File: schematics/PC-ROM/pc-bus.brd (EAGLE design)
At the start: 152.4 x 138.4 mm, 20 parts

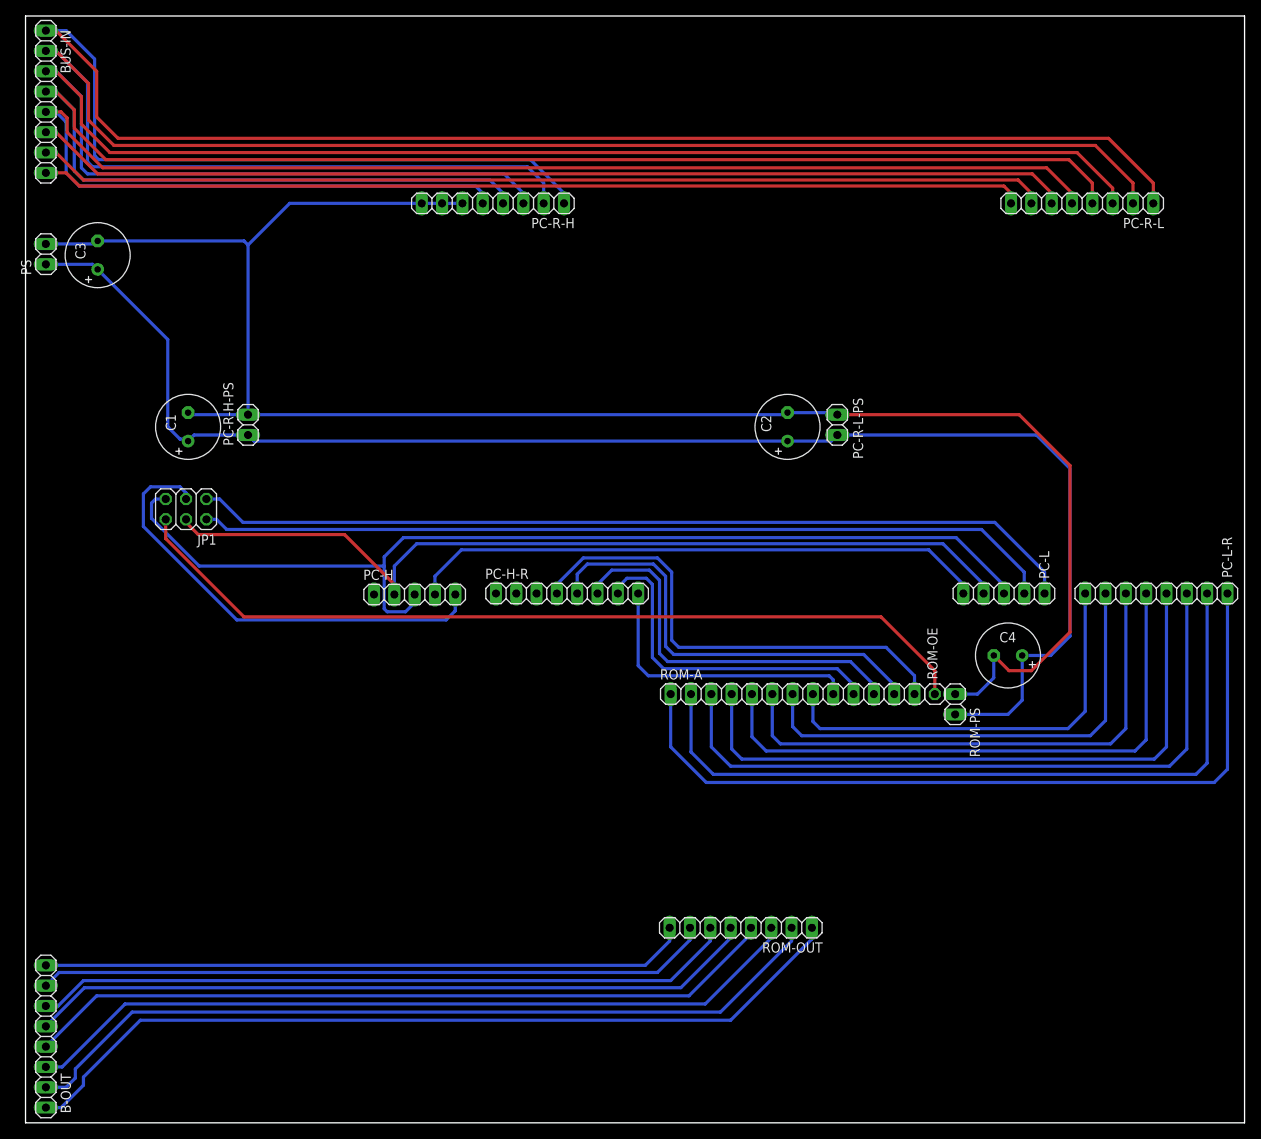
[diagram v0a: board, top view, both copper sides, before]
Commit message: Added resistors to rom address.
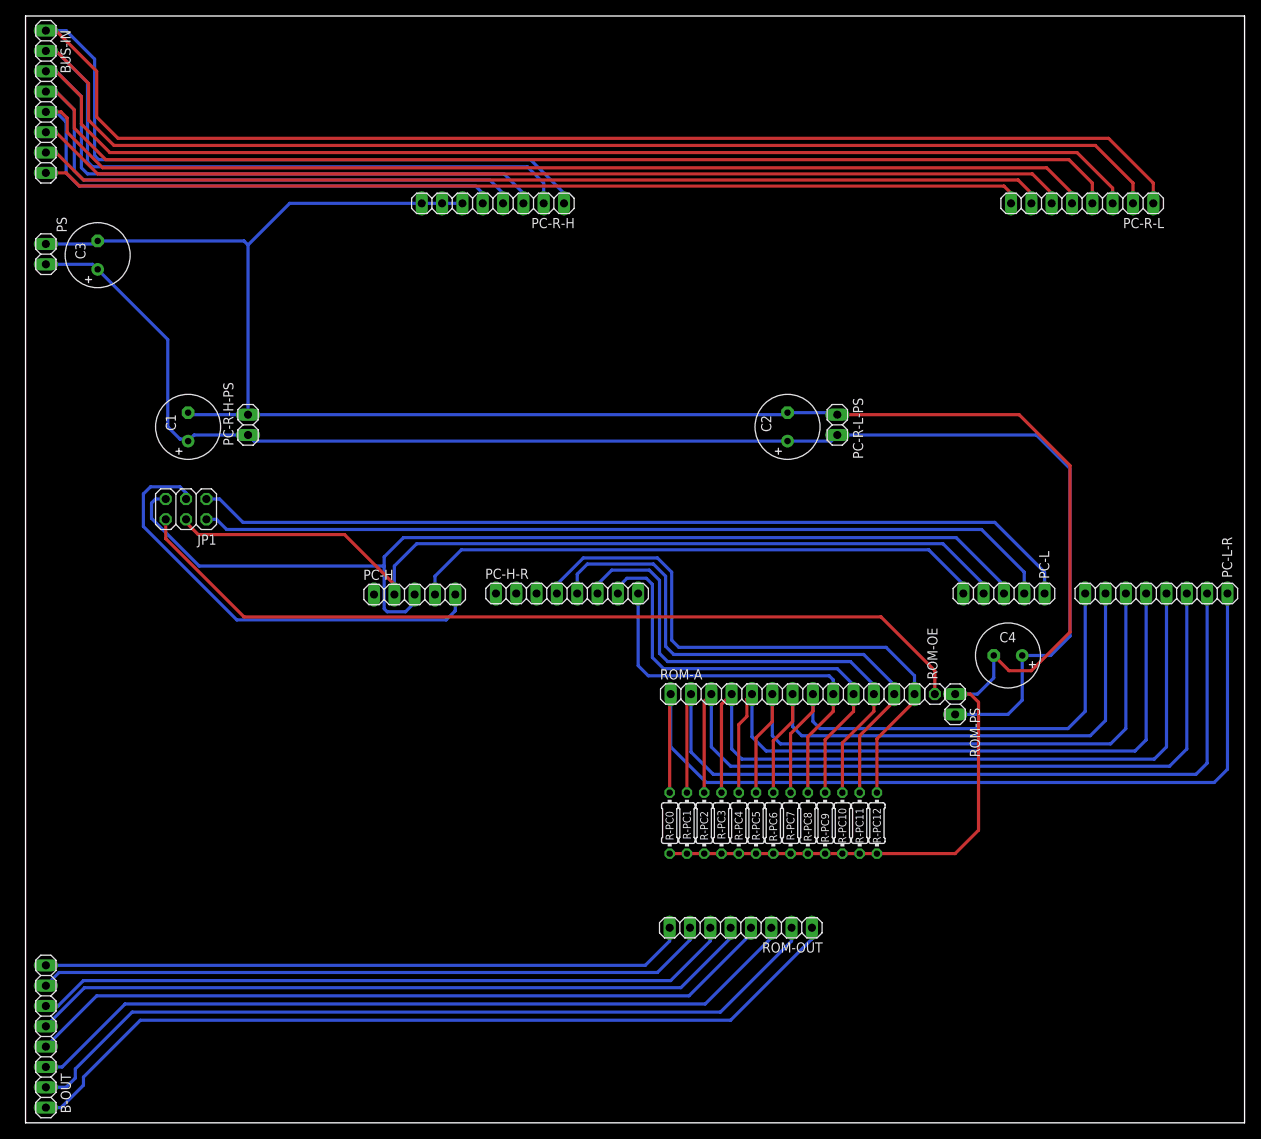
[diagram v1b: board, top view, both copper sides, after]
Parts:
- added R-PC0, R-PC1, R-PC10, R-PC11, R-PC12, R-PC2, R-PC3, R-PC4, R-PC5, R-PC6, R-PC7, R-PC8, R-PC9: (no value), rcl:0204/7
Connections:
- net GND: now also R-PC0.1, R-PC1.1, R-PC10.1, R-PC11.1, R-PC12.1, R-PC2.1, R-PC3.1, R-PC4.1, R-PC5.1, R-PC6.1, R-PC7.1, R-PC8.1, R-PC9.1
- net PC0: now also R-PC0.2
- net PC1: now also R-PC1.2
- net PC10: now also R-PC10.2
- net PC11: now also R-PC11.2
- net PC12: now also R-PC12.2
- net PC2: now also R-PC2.2
- net PC3: now also R-PC3.2
- net PC4: now also R-PC4.2
- net PC5: now also R-PC5.2
- net PC6: now also R-PC6.2
- net PC7: now also R-PC7.2
- net PC8: now also R-PC8.2
- net PC9: now also R-PC9.2
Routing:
- net GND: track 230.6 -> 289.8 mm
- net PC12: track 60.6 -> 74.9 mm
- net PC11: track 55.1 -> 69.2 mm
- net PC10: track 48.9 -> 62.8 mm
- net PC9: track 42.7 -> 56.5 mm
- net PC8: track 35.9 -> 49.5 mm
- net PC7: track 53.5 -> 66.9 mm
- net PC6: track 60.3 -> 73.6 mm
- net PC5: track 67.5 -> 80.7 mm
- net PC4: track 74.2 -> 87.2 mm
- net PC3: track 81.5 -> 94.4 mm
- net PC2: track 87.4 -> 100.1 mm
- net PC1: track 94.7 -> 107.2 mm
- net PC0: track 100.7 -> 113.1 mm
